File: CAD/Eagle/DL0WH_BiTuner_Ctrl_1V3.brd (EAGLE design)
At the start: 96.5 x 73 mm, 157 parts, among them Q0321 ABS07-32.768KHZ, U0101 STM32L476RXT_64PIN_LDO, U0601 MC33996, U0701 MC33996, U0801 MC33996, U0921 TS5A23166, U0941 LM2611, U0951 OPA354, U0961 OPA354, U0962 MCP4661-103E-MS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

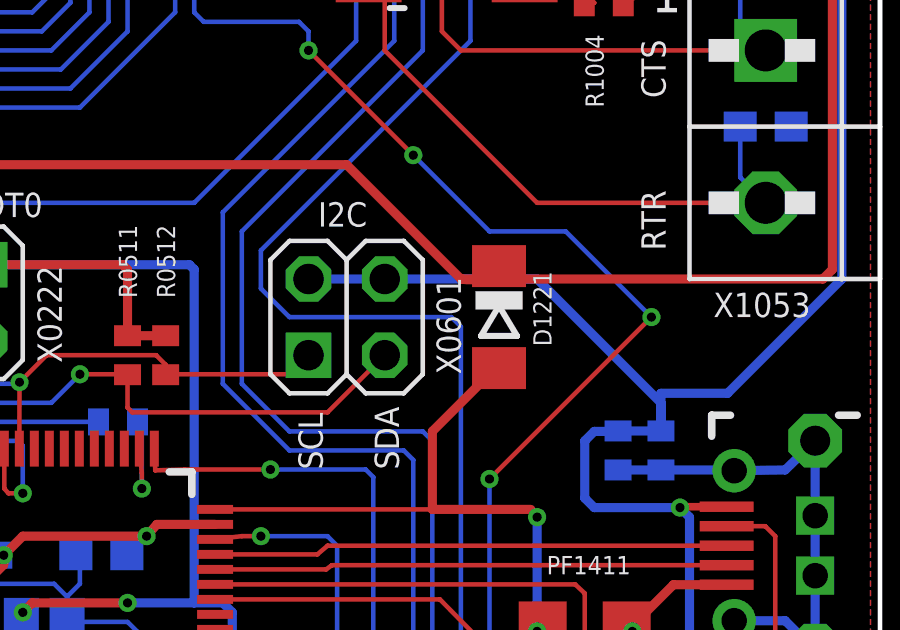
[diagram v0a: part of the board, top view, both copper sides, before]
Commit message: HW_1V3 - CAD/Eagle - Rename X0601 to X0501
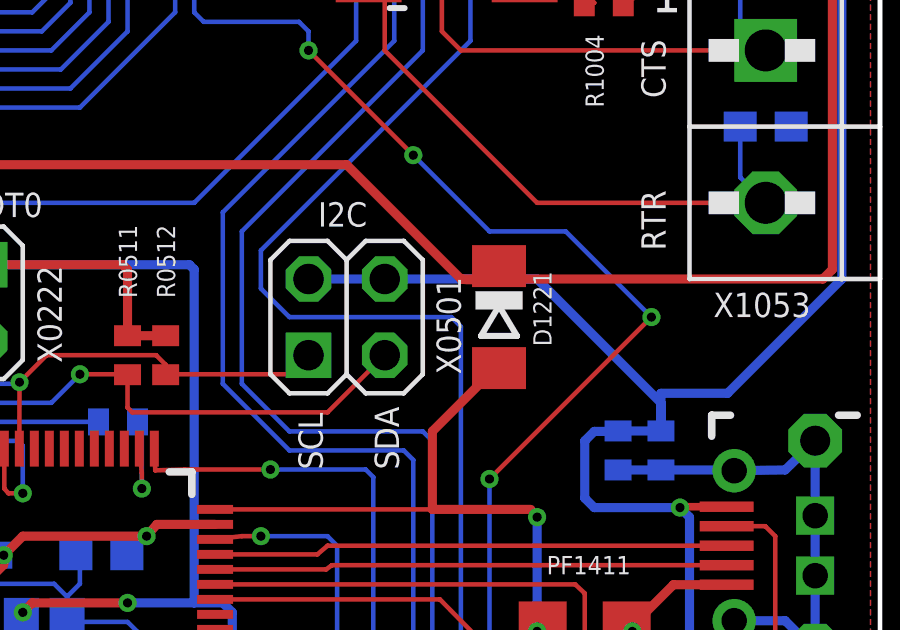
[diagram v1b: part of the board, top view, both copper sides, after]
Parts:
- renumbered X0601 to X0501
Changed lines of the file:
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@@
 <attribute name="VALUE" x="13.6525" y="28.2575" size="0.6096" layer="27" font="vector" ratio="10" rot="R270"/>
 </element>
-<element name="X0601" library="df4iah_connector" package="2X02" value="" x="78.74" y="29.21" smashed="yes">
+<element name="X0501" library="df4iah_connector" package="2X02" value="" x="78.74" y="29.21" smashed="yes">
 <attribute name="NAME" x="82.55" y="27.305" size="0.8128" layer="25" font="vector" ratio="15" rot="R90"/>
 <attribute name="VALUE" x="74.93" y="24.765" size="1.27" layer="27"/>
@@
 <contactref element="U0951" pad="3"/>
 <contactref element="D0971" pad="C"/>
-<contactref element="X0601" pad="2"/>
-<contactref element="X0601" pad="4"/>
+<contactref element="X0501" pad="2"/>
+<contactref element="X0501" pad="4"/>
 <contactref element="R0901" pad="1"/>
 <contactref element="R0911" pad="1"/>
@@
 <contactref element="U0101" pad="58"/>
 <contactref element="R0512" pad="1"/>
-<contactref element="X0601" pad="1"/>
+<contactref element="X0501" pad="1"/>
 <wire x1="77.47" y1="27.94" x2="76.835" y2="27.305" width="0.1524" layer="1"/>
 <wire x1="76.835" y1="27.305" x2="72.7225" y2="27.305" width="0.1524" layer="1"/>
@@
 <contactref element="U0101" pad="62"/>
 <contactref element="R0511" pad="1"/>
-<contactref element="X0601" pad="3"/>
+<contactref element="X0501" pad="3"/>
 <wire x1="80.01" y1="27.94" x2="78.105" y2="26.035" width="0.1524" layer="1"/>
 <wire x1="78.105" y1="26.035" x2="71.59625" y2="26.035" width="0.1524" layer="1"/>

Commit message: HW_1V3 - CAD/Eagle - MCU name fixed
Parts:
- U0101: value STM32L476RXT_64PIN_LDO -> STM32L476RGT6_64PIN_LDO
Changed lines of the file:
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@@
 <layer number="17" name="Pads" color="2" fill="1" visible="yes" active="yes"/>
 <layer number="18" name="Vias" color="2" fill="1" visible="yes" active="yes"/>
-<layer number="19" name="Unrouted" color="6" fill="1" visible="yes" active="yes"/>
+<layer number="19" name="Unrouted" color="6" fill="1" visible="no" active="yes"/>
 <layer number="20" name="Dimension" color="5" fill="1" visible="yes" active="yes"/>
-<layer number="21" name="tPlace" color="7" fill="1" visible="yes" active="yes"/>
-<layer number="22" name="bPlace" color="7" fill="1" visible="yes" active="yes"/>
+<layer number="21" name="tPlace" color="7" fill="1" visible="no" active="yes"/>
+<layer number="22" name="bPlace" color="7" fill="1" visible="no" active="yes"/>
 <layer number="23" name="tOrigins" color="15" fill="1" visible="yes" active="yes"/>
 <layer number="24" name="bOrigins" color="15" fill="1" visible="yes" active="yes"/>
-<layer number="25" name="tNames" color="7" fill="1" visible="yes" active="yes"/>
-<layer number="26" name="bNames" color="7" fill="1" visible="yes" active="yes"/>
+<layer number="25" name="tNames" color="7" fill="1" visible="no" active="yes"/>
+<layer number="26" name="bNames" color="7" fill="1" visible="no" active="yes"/>
 <layer number="27" name="tValues" color="7" fill="1" visible="no" active="yes"/>
 <layer number="28" name="bValues" color="7" fill="1" visible="no" active="yes"/>
-<layer number="29" name="tStop" color="7" fill="3" visible="yes" active="yes"/>
-<layer number="30" name="bStop" color="7" fill="6" visible="yes" active="yes"/>
-<layer number="31" name="tCream" color="7" fill="4" visible="yes" active="yes"/>
-<layer number="32" name="bCream" color="7" fill="5" visible="yes" active="yes"/>
+<layer number="29" name="tStop" color="7" fill="3" visible="no" active="yes"/>
+<layer number="30" name="bStop" color="7" fill="6" visible="no" active="yes"/>
+<layer number="31" name="tCream" color="7" fill="4" visible="no" active="yes"/>
+<layer number="32" name="bCream" color="7" fill="5" visible="no" active="yes"/>
 <layer number="33" name="tFinish" color="6" fill="3" visible="no" active="yes"/>
 <layer number="34" name="bFinish" color="6" fill="6" visible="no" active="yes"/>
@@
 <layer number="42" name="bRestrict" color="1" fill="10" visible="no" active="yes"/>
 <layer number="43" name="vRestrict" color="2" fill="10" visible="no" active="yes"/>
-<layer number="44" name="Drills" color="7" fill="1" visible="yes" active="yes"/>
+<layer number="44" name="Drills" color="7" fill="1" visible="no" active="yes"/>
 <layer number="45" name="Holes" color="7" fill="1" visible="no" active="yes"/>
-<layer number="46" name="Milling" color="3" fill="1" visible="yes" active="yes"/>
+<layer number="46" name="Milling" color="3" fill="1" visible="no" active="yes"/>
 <layer number="47" name="Measures" color="13" fill="1" visible="no" active="yes"/>
 <layer number="48" name="Document" color="7" fill="1" visible="no" active="yes"/>
-<layer number="49" name="Reference" color="7" fill="1" visible="yes" active="yes"/>
+<layer number="49" name="Reference" color="7" fill="1" visible="no" active="yes"/>
 <layer number="50" name="dxf" color="7" fill="1" visible="no" active="no"/>
-<layer number="51" name="tDocu" color="14" fill="1" visible="yes" active="yes"/>
-<layer number="52" name="bDocu" color="6" fill="1" visible="yes" active="yes"/>
+<layer number="51" name="tDocu" color="14" fill="1" visible="no" active="yes"/>
+<layer number="52" name="bDocu" color="6" fill="1" visible="no" active="yes"/>
 <layer number="53" name="tGND_GNDA" color="7" fill="9" visible="no" active="no"/>
 <layer number="54" name="bGND_GNDA" color="1" fill="9" visible="no" active="no"/>
@@
 <attribute name="VALUE" x="-0.3175" y="52.705" size="0.6096" layer="27" font="vector" ratio="10" rot="R90"/>
 </element>
-<element name="U0101" library="df4iah_stm32l4" package="LQFP64" value="STM32L476RXT_64PIN_LDO" x="68.58" y="19.05" smashed="yes">
+<element name="U0101" library="df4iah_stm32l4" package="LQFP64" value="STM32L476RGT6_64PIN_LDO" x="68.58" y="19.05" smashed="yes">
 <attribute name="NAME" x="62.50375" y="23.3775" size="0.8128" layer="25" rot="R90"/>
 <attribute name="VALUE" x="65.555" y="16.6" size="0.8128" layer="27"/>

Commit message: HW_1V3 - CAD/Eagle - renaming fix, jumper replaced by 0R bridge
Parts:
- removed C0054: 10nF, df4iah_rcl:C0603
- removed SJ0401: (no value), df4iah_jumper:SJ
- added C1054: 10nF, df4iah_rcl:C0402
- added R0401: 0R, df4iah_rcl:R0402
- C0942: device df4iah_rcl:C0805 -> df4iah_rcl:C0603
- C1051, C1052, C1053, C1151, C1152, C1153, C1154: device df4iah_rcl:C0603 -> df4iah_rcl:C0402
- R0962: value 1.0kR -> 1kR
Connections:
- net +3V3: now also R0401.1; no longer SJ0401.1
- net GND: now also C1054.2; no longer C0054.2
- net MCU_VDD: now also R0401.2; no longer SJ0401.2
- net RS_DTE_RTR: now also C1054.1; no longer C0054.1
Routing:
- net GND: track 902.4 -> 904.0 mm

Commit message: HW_1V3 - CAD/Eagle - PMIC CUK additional soft-start, OpAmp output w/ higher resistor
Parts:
- added C0949: 100nF, df4iah_rcl:C0402
- added R0949: 100kR, df4iah_rcl:R0402
- R0972: value 47R -> 1kR
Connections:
- new net LM_SHDN: C0949.1, R0949.2, U0941.4
- net +3V3: now also R0949.1; no longer U0941.4
- net -1V5: now also C0949.2
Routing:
- net +3V3: track 240.8 -> 237.8 mm
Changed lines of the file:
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@@
 <layer number="19" name="Unrouted" color="6" fill="1" visible="no" active="yes"/>
 <layer number="20" name="Dimension" color="5" fill="1" visible="yes" active="yes"/>
-<layer number="21" name="tPlace" color="7" fill="1" visible="no" active="yes"/>
-<layer number="22" name="bPlace" color="7" fill="1" visible="no" active="yes"/>
+<layer number="21" name="tPlace" color="7" fill="1" visible="yes" active="yes"/>
+<layer number="22" name="bPlace" color="7" fill="1" visible="yes" active="yes"/>
 <layer number="23" name="tOrigins" color="15" fill="1" visible="yes" active="yes"/>
 <layer number="24" name="bOrigins" color="15" fill="1" visible="yes" active="yes"/>
@@
 <attribute name="VALUE" x="13.97" y="25.4" size="0.6096" layer="27" font="vector" ratio="10" rot="R90"/>
 </element>
-<element name="R0972" library="df4iah_rcl" package="R0402" value="47R" x="15.875" y="20.955" smashed="yes" rot="MR90">
+<element name="R0972" library="df4iah_rcl" package="R0402" value="1kR" x="15.875" y="20.955" smashed="yes" rot="MR90">
 <attribute name="NAME" x="16.98625" y="20.0025" size="0.6096" layer="26" font="vector" ratio="10" rot="MR90"/>
 <attribute name="VALUE" x="14.2875" y="19.3675" size="0.6096" layer="28" font="vector" ratio="10" rot="MR90"/>
@@
 <attribute name="VALUE" x="12.7" y="12.3825" size="0.6096" layer="28" font="vector" ratio="10" rot="MR0"/>
 </element>
+<element name="C0949" library="df4iah_rcl" package="C0402" value="100nF" x="-3.81" y="-24.13"/>
+<element name="R0949" library="df4iah_rcl" package="R0402" value="100kR" x="-3.81" y="-29.21"/>
 </elements>
 <signals>
@@
 <contactref element="U0961" pad="5"/>
 <contactref element="U0941" pad="5"/>
-<contactref element="U0941" pad="4"/>
 <contactref element="C0941" pad="1"/>
 <contactref element="L0941" pad="2"/>
@@
 <wire x1="24.4221" y1="34.11855" x2="22.28125" y2="34.11855" width="0.3048" layer="16"/>
 <wire x1="22.28125" y1="34.11855" x2="22.28125" y2="34.13125" width="0.1524" layer="16"/>
-<wire x1="24.4221" y1="34.11855" x2="24.4221" y2="32.23895" width="0.3048" layer="16"/>
 <via x="23.33625" y="32.22625" extent="1-16" drill="0.3"/>
 <wire x1="23.33625" y1="32.22625" x2="24.56125" y2="32.22625" width="0.3048" layer="1"/>
-<wire x1="24.4221" y1="32.23895" x2="23.34895" y2="32.23895" width="0.3048" layer="16"/>
 <wire x1="23.34895" y1="32.23895" x2="23.33625" y2="32.22625" width="0.3048" layer="16"/>
 <wire x1="24.56125" y1="32.22625" x2="25.0375" y2="31.75" width="0.3048" layer="1"/>
@@
 <wire x1="17.62125" y1="21.73605" x2="17.62125" y2="23.33625" width="0.254" layer="1"/>
 <wire x1="17.62125" y1="23.33625" x2="16.66875" y2="24.28875" width="0.254" layer="1"/>
+<contactref element="R0949" pad="1"/>
+<wire x1="25.4" y1="33.02" x2="24.4221" y2="34.11855" width="0" layer="19" extent="1-16"/>
+<wire x1="-4.46" y1="-29.21" x2="13.91" y2="10.725" width="0" layer="19" extent="1-16"/>
 </signal>
 <signal name="P$8">
@@
 <wire x1="20.32" y1="26.67" x2="16.66875" y2="23.01875" width="0.3048" layer="16"/>
 <via x="16.66875" y="23.01875" extent="1-16" drill="0.3"/>
+<contactref element="C0949" pad="2"/>
+<wire x1="-3.16" y1="-24.13" x2="12.7" y2="20.3454" width="0" layer="19" extent="1-1"/>
 </signal>
 <signal name="SWR_OP2_IN">
@@
 <wire x1="19.04" y1="10.795" x2="19.11" y2="10.725" width="0.1524" layer="16"/>
 </signal>
+<signal name="LM_SHDN">
+<contactref element="U0941" pad="4"/>
+<contactref element="R0949" pad="2"/>
+<contactref element="C0949" pad="1"/>
+<wire x1="-4.46" y1="-24.13" x2="24.4221" y2="32.23895" width="0" layer="19" extent="1-16"/>
+<wire x1="-3.16" y1="-29.21" x2="-4.46" y2="-24.13" width="0" layer="19" extent="1-1"/>
+</signal>
 </signals>

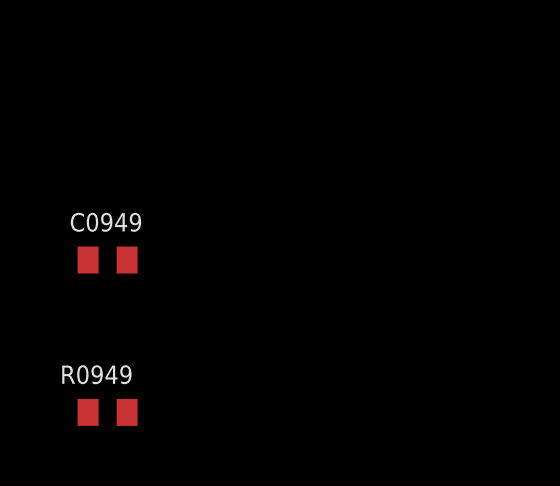
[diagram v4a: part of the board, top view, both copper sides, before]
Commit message: HW_1V3 - CAD/Eagle - soft-start not neded, prog. potis nominal values added
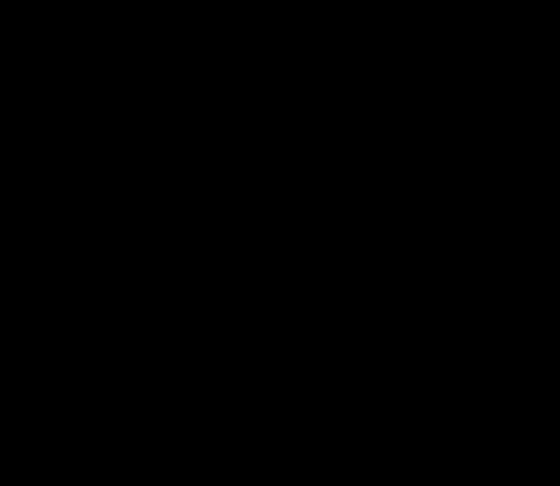
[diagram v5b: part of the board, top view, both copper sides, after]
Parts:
- removed C0949: 100nF, df4iah_rcl:C0402
- removed R0949: 100kR, df4iah_rcl:R0402
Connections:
- removed net LM_SHDN: C0949.1, R0949.2, U0941.4
- net +3V3: now also U0941.4; no longer R0949.1
- net -1V5: no longer C0949.2
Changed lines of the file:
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@@
 <layer number="17" name="Pads" color="2" fill="1" visible="yes" active="yes"/>
 <layer number="18" name="Vias" color="2" fill="1" visible="yes" active="yes"/>
-<layer number="19" name="Unrouted" color="6" fill="1" visible="no" active="yes"/>
+<layer number="19" name="Unrouted" color="6" fill="1" visible="yes" active="yes"/>
 <layer number="20" name="Dimension" color="5" fill="1" visible="yes" active="yes"/>
 <layer number="21" name="tPlace" color="7" fill="1" visible="yes" active="yes"/>
@@
 <attribute name="VALUE" x="12.7" y="12.3825" size="0.6096" layer="28" font="vector" ratio="10" rot="MR0"/>
 </element>
-<element name="C0949" library="df4iah_rcl" package="C0402" value="100nF" x="-3.81" y="-24.13"/>
-<element name="R0949" library="df4iah_rcl" package="R0402" value="100kR" x="-3.81" y="-29.21"/>
 </elements>
 <signals>
@@
 <wire x1="17.62125" y1="21.73605" x2="17.62125" y2="23.33625" width="0.254" layer="1"/>
 <wire x1="17.62125" y1="23.33625" x2="16.66875" y2="24.28875" width="0.254" layer="1"/>
-<contactref element="R0949" pad="1"/>
+<contactref element="U0941" pad="4"/>
 <wire x1="25.4" y1="33.02" x2="24.4221" y2="34.11855" width="0" layer="19" extent="1-16"/>
-<wire x1="-4.46" y1="-29.21" x2="13.91" y2="10.725" width="0" layer="19" extent="1-16"/>
+<wire x1="24.4221" y1="32.23895" x2="24.56125" y2="32.22625" width="0" layer="19" extent="1-16"/>
 </signal>
 <signal name="P$8">
@@
 <wire x1="20.32" y1="26.67" x2="16.66875" y2="23.01875" width="0.3048" layer="16"/>
 <via x="16.66875" y="23.01875" extent="1-16" drill="0.3"/>
-<contactref element="C0949" pad="2"/>
-<wire x1="-3.16" y1="-24.13" x2="12.7" y2="20.3454" width="0" layer="19" extent="1-1"/>
 </signal>
 <signal name="SWR_OP2_IN">
@@
 <wire x1="19.04" y1="10.795" x2="19.11" y2="10.725" width="0.1524" layer="16"/>
 </signal>
-<signal name="LM_SHDN">
-<contactref element="U0941" pad="4"/>
-<contactref element="R0949" pad="2"/>
-<contactref element="C0949" pad="1"/>
-<wire x1="-4.46" y1="-24.13" x2="24.4221" y2="32.23895" width="0" layer="19" extent="1-16"/>
-<wire x1="-3.16" y1="-29.21" x2="-4.46" y2="-24.13" width="0" layer="19" extent="1-1"/>
-</signal>
 </signals>
